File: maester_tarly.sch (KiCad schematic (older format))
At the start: 30 parts, among them J101 Micro_SD_Card_Det, J102 USB_B_Micro, J103 USB_A, J104 Conn_01x06, J105 Conn_01x10, J106 RJ45_Amphenol_RJMG1BD3B8K1ANR, J107 DF40GB(1.5)-48DS-0.4V, J108 DF40GB(1.5)-48DS-0.4V, J109 DF40GB(1.5)-48DS-0.4V, J110 DF40GB(1.5)-48DS-0.4V

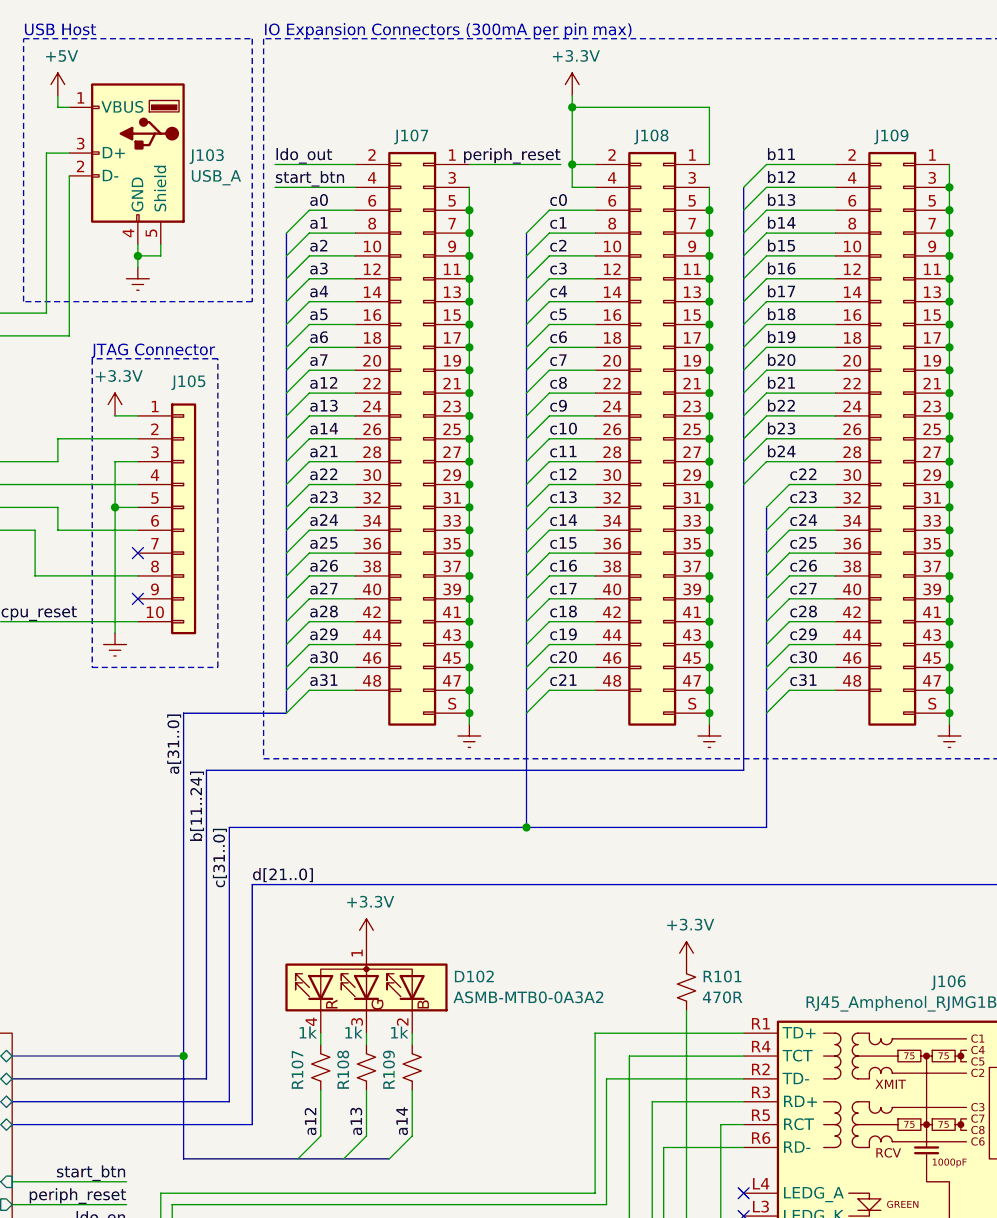
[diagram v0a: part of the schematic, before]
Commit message: Escaped all traced from the CPU
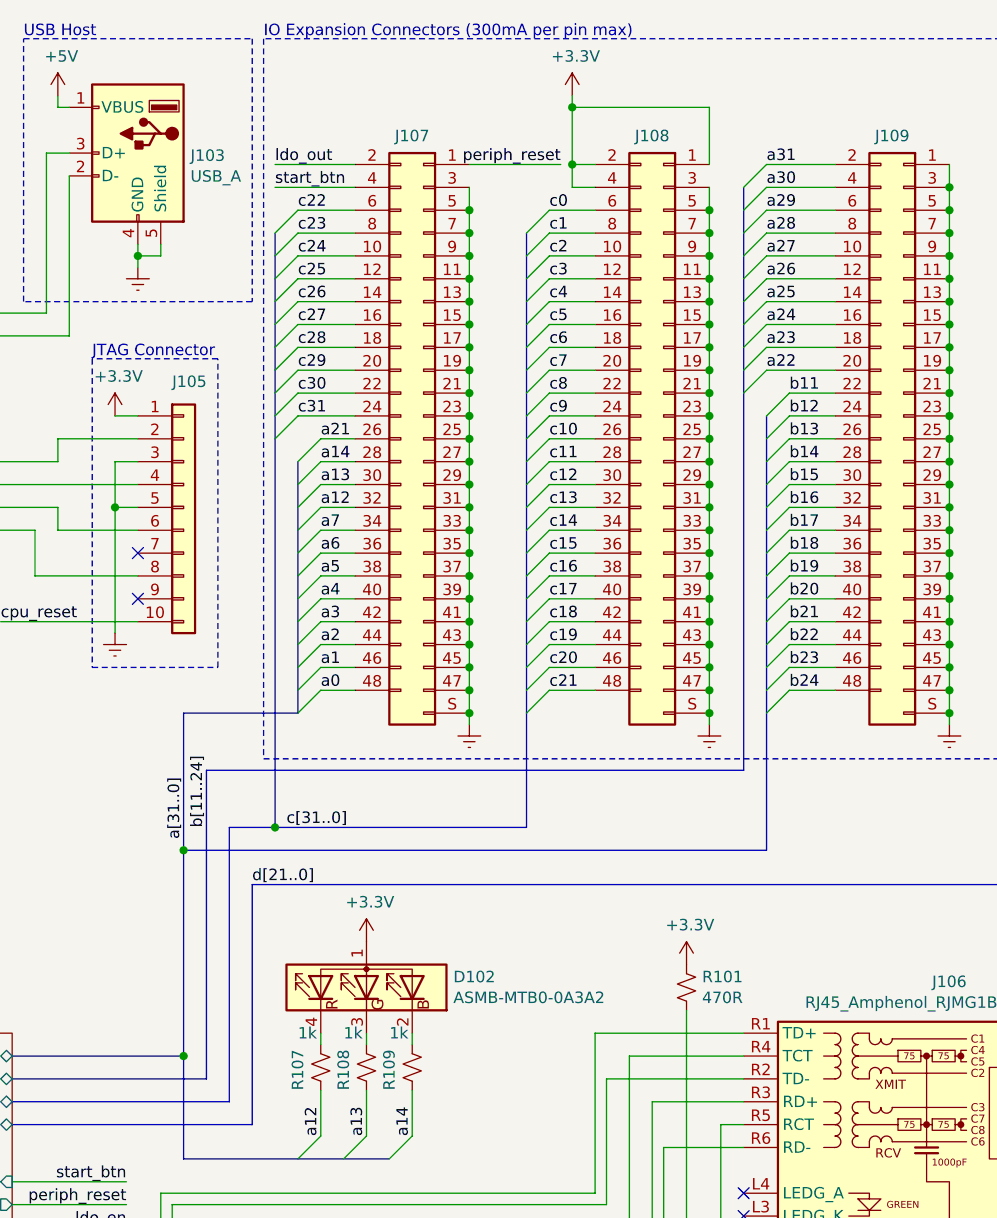
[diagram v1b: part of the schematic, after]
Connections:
- net a0: now also J107.48 (Pin_48); no longer J107.6 (Pin_6)
- net a1: now also J107.46 (Pin_46); no longer J107.8 (Pin_8)
- net a12: now also J107.32 (Pin_32); no longer J107.22 (Pin_22)
- net a13: now also J107.30 (Pin_30); no longer J107.24 (Pin_24)
- net a14: now also J107.28 (Pin_28); no longer J107.26 (Pin_26)
- net a2: now also J107.44 (Pin_44); no longer J107.10 (Pin_10)
- net a21: now also J107.26 (Pin_26); no longer J107.28 (Pin_28)
- net a22: now also J109.20 (Pin_20); no longer J107.30 (Pin_30)
- net a23: now also J109.18 (Pin_18); no longer J107.32 (Pin_32)
- net a24: now also J109.16 (Pin_16); no longer J107.34 (Pin_34)
- net a25: now also J109.14 (Pin_14); no longer J107.36 (Pin_36)
- net a26: now also J109.12 (Pin_12); no longer J107.38 (Pin_38)
- net a27: now also J109.10 (Pin_10); no longer J107.40 (Pin_40)
- net a28: now also J109.8 (Pin_8); no longer J107.42 (Pin_42)
- net a29: now also J109.6 (Pin_6); no longer J107.44 (Pin_44)
- net a3: now also J107.42 (Pin_42); no longer J107.12 (Pin_12)
- net a30: now also J109.4 (Pin_4); no longer J107.46 (Pin_46)
- net a31: now also J109.2 (Pin_2); no longer J107.48 (Pin_48)
- net a4: now also J107.40 (Pin_40); no longer J107.14 (Pin_14)
- net a5: now also J107.38 (Pin_38); no longer J107.16 (Pin_16)
- net a6: now also J107.36 (Pin_36); no longer J107.18 (Pin_18)
- net a7: now also J107.34 (Pin_34); no longer J107.20 (Pin_20)
- net b11: now also J109.22 (Pin_22); no longer J109.2 (Pin_2)
- net b12: now also J109.24 (Pin_24); no longer J109.4 (Pin_4)
- net b13: now also J109.26 (Pin_26); no longer J109.6 (Pin_6)
- net b14: now also J109.28 (Pin_28); no longer J109.8 (Pin_8)
- net b15: now also J109.30 (Pin_30); no longer J109.10 (Pin_10)
- net b16: now also J109.32 (Pin_32); no longer J109.12 (Pin_12)
- net b17: now also J109.34 (Pin_34); no longer J109.14 (Pin_14)
- net b18: now also J109.36 (Pin_36); no longer J109.16 (Pin_16)
- net b19: now also J109.38 (Pin_38); no longer J109.18 (Pin_18)
- net b20: now also J109.40 (Pin_40); no longer J109.20 (Pin_20)
- net b21: now also J109.42 (Pin_42); no longer J109.22 (Pin_22)
- net b22: now also J109.44 (Pin_44); no longer J109.24 (Pin_24)
- net b23: now also J109.46 (Pin_46); no longer J109.26 (Pin_26)
- net b24: now also J109.48 (Pin_48); no longer J109.28 (Pin_28)
- net c22: now also J107.6 (Pin_6); no longer J109.30 (Pin_30)
- net c23: now also J107.8 (Pin_8); no longer J109.32 (Pin_32)
- net c24: now also J107.10 (Pin_10); no longer J109.34 (Pin_34)
- net c25: now also J107.12 (Pin_12); no longer J109.36 (Pin_36)
- net c26: now also J107.14 (Pin_14); no longer J109.38 (Pin_38)
- net c27: now also J107.16 (Pin_16); no longer J109.40 (Pin_40)
- net c28: now also J107.18 (Pin_18); no longer J109.42 (Pin_42)
- net c29: now also J107.20 (Pin_20); no longer J109.44 (Pin_44)
- net c30: now also J107.22 (Pin_22); no longer J109.46 (Pin_46)
- net c31: now also J107.24 (Pin_24); no longer J109.48 (Pin_48)

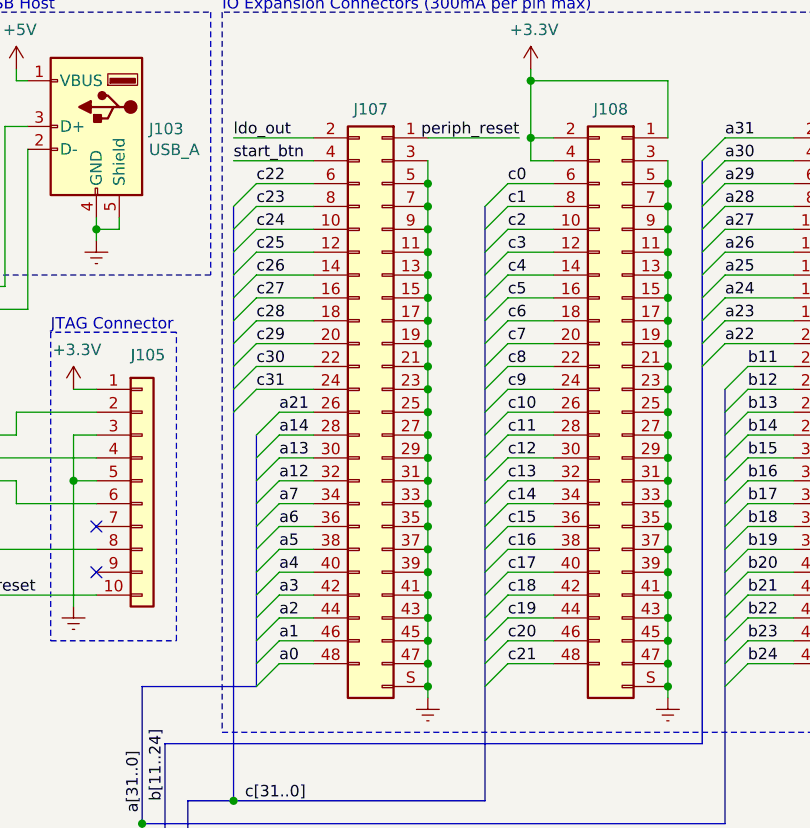
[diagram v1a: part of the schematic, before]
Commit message: Placed all the parts. Some will have to move.
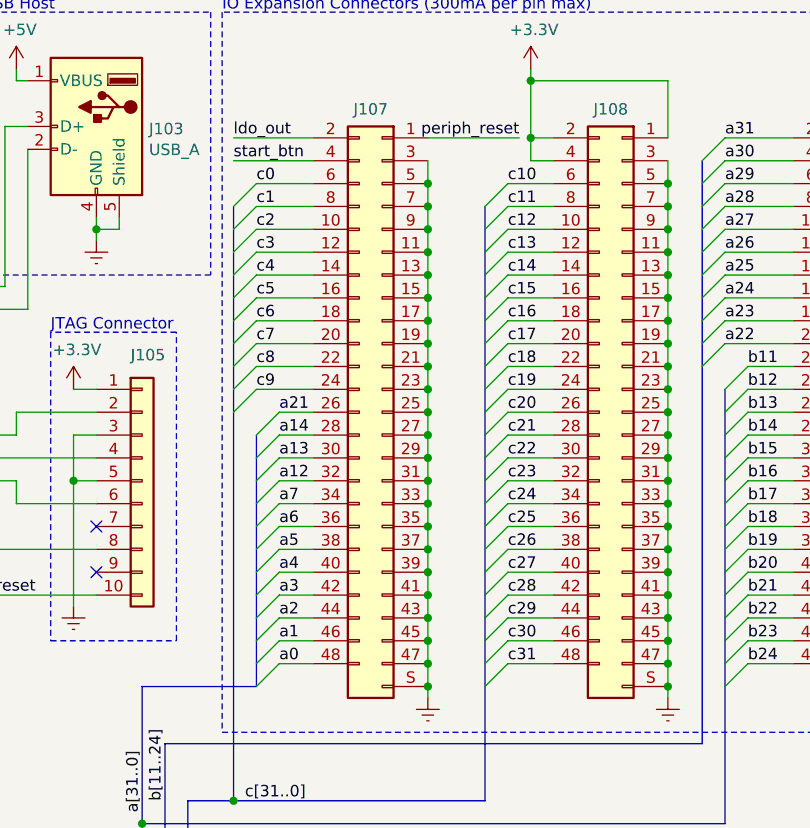
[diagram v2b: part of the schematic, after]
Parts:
- C102: footprint Capacitor_SMD:C_0402_1005Metric -> Capacitor_SMD:C_0805_2012Metric
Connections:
- net c0: now also J107.6 (Pin_6); no longer J108.6 (Pin_6)
- net c1: now also J107.8 (Pin_8); no longer J108.8 (Pin_8)
- net c10: now also J108.6 (Pin_6); no longer J108.26 (Pin_26)
- net c11: now also J108.8 (Pin_8); no longer J108.28 (Pin_28)
- net c12: now also J108.10 (Pin_10); no longer J108.30 (Pin_30)
- net c13: now also J108.12 (Pin_12); no longer J108.32 (Pin_32)
- net c14: now also J108.14 (Pin_14); no longer J108.34 (Pin_34)
- net c15: now also J108.16 (Pin_16); no longer J108.36 (Pin_36)
- net c16: now also J108.18 (Pin_18); no longer J108.38 (Pin_38)
- net c17: now also J108.20 (Pin_20); no longer J108.40 (Pin_40)
- net c18: now also J108.22 (Pin_22); no longer J108.42 (Pin_42)
- net c19: now also J108.24 (Pin_24); no longer J108.44 (Pin_44)
- net c2: now also J107.10 (Pin_10); no longer J108.10 (Pin_10)
- net c20: now also J108.26 (Pin_26); no longer J108.46 (Pin_46)
- net c21: now also J108.28 (Pin_28); no longer J108.48 (Pin_48)
- net c22: now also J108.30 (Pin_30); no longer J107.6 (Pin_6)
- net c23: now also J108.32 (Pin_32); no longer J107.8 (Pin_8)
- net c24: now also J108.34 (Pin_34); no longer J107.10 (Pin_10)
- net c25: now also J108.36 (Pin_36); no longer J107.12 (Pin_12)
- net c26: now also J108.38 (Pin_38); no longer J107.14 (Pin_14)
- net c27: now also J108.40 (Pin_40); no longer J107.16 (Pin_16)
- net c28: now also J108.42 (Pin_42); no longer J107.18 (Pin_18)
- net c29: now also J108.44 (Pin_44); no longer J107.20 (Pin_20)
- net c3: now also J107.12 (Pin_12); no longer J108.12 (Pin_12)
- net c30: now also J108.46 (Pin_46); no longer J107.22 (Pin_22)
- net c31: now also J108.48 (Pin_48); no longer J107.24 (Pin_24)
- net c4: now also J107.14 (Pin_14); no longer J108.14 (Pin_14)
- net c5: now also J107.16 (Pin_16); no longer J108.16 (Pin_16)
- net c6: now also J107.18 (Pin_18); no longer J108.18 (Pin_18)
- net c7: now also J107.20 (Pin_20); no longer J108.20 (Pin_20)
- net c8: now also J107.22 (Pin_22); no longer J108.22 (Pin_22)
- net c9: now also J107.24 (Pin_24); no longer J108.24 (Pin_24)
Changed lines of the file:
@@
 F 0 "C102" H 3392 5846 50  0000 L CNN
 F 1 "4.7uF" H 3392 5755 50  0000 L CNN
-F 2 "Capacitor_SMD:C_0402_1005Metric" H 3300 5800 50  0001 C CNN
+F 2 "Capacitor_SMD:C_0805_2012Metric" H 3300 5800 50  0001 C CNN
 F 3 "~" H 3300 5800 50  0001 C CNN
 	1    3300 5800
@@
 Text Label 6800 4100 1    50   ~ 0
 b[11..24]
+Text Label 7200 1400 0    50   ~ 0
+c0
+Text Label 7200 1500 0    50   ~ 0
+c1
+Text Label 7200 1600 0    50   ~ 0
+c2
+Text Label 7200 1700 0    50   ~ 0
+c3
+Text Label 7200 1800 0    50   ~ 0
+c4
+Text Label 7200 1900 0    50   ~ 0
+c5
+Text Label 7200 2000 0    50   ~ 0
+c6
+Text Label 7200 2100 0    50   ~ 0
+c7
+Text Label 7200 2200 0    50   ~ 0
+c8
+Text Label 7200 2300 0    50   ~ 0
+c9
 Text Label 8300 1400 0    50   ~ 0
-c0
+c10
 Text Label 8300 1500 0    50   ~ 0
-c1
+c11
 Text Label 8300 1600 0    50   ~ 0
-c2
+c12
 Text Label 8300 1700 0    50   ~ 0
-c3
+c13
 Text Label 8300 1800 0    50   ~ 0
-c4
+c14
 Text Label 8300 1900 0    50   ~ 0
-c5
+c15
 Text Label 8300 2000 0    50   ~ 0
-c6
+c16
 Text Label 8300 2100 0    50   ~ 0
-c7
+c17
 Text Label 8300 2200 0    50   ~ 0
-c8
+c18
 Text Label 8300 2300 0    50   ~ 0
-c9
+c19
 Text Label 8300 2400 0    50   ~ 0
-c10
+c20
 Text Label 8300 2500 0    50   ~ 0
-c11
-Text Label 8300 2600 0    50   ~ 0
-c12
-Text Label 8300 2700 0    50   ~ 0
-c13
-Text Label 8300 2800 0    50   ~ 0
-c14
-Text Label 8300 2900 0    50   ~ 0
-c15
-Text Label 8300 3000 0    50   ~ 0
-c16
-Text Label 8300 3100 0    50   ~ 0
-c17
-Text Label 8300 3200 0    50   ~ 0
-c18
-Text Label 8300 3300 0    50   ~ 0
-c19
-Text Label 8300 3400 0    50   ~ 0
-c20
-Text Label 8300 3500 0    50   ~ 0
 c21
-Text Label 7200 1400 0    50   ~ 0
-c22
-Text Label 7200 1500 0    50   ~ 0
-c23
-Text Label 7200 1600 0    50   ~ 0
-c24
-Text Label 7200 1700 0    50   ~ 0
-c25
-Text Label 7200 1800 0    50   ~ 0
-c26
-Text Label 7200 1900 0    50   ~ 0
-c27
-Text Label 7200 2000 0    50   ~ 0
-c28
-Text Label 7200 2100 0    50   ~ 0
-c29
-Text Label 7200 2200 0    50   ~ 0
-c30
-Text Label 7200 2300 0    50   ~ 0
-c31
 Wire Wire Line
 	6100 1150 6200 1150
@@
 	7450 3500 7300 3500
 Wire Wire Line
-	8500 3400 8300 3400
-Wire Wire Line
-	8500 3500 8300 3500
+	8500 2400 8300 2400
+Wire Wire Line
+	8500 2500 8300 2500
 Wire Wire Line
 	8500 1400 8300 1400
@@
 Wire Wire Line
 	8500 2300 8300 2300
-Wire Wire Line
-	8500 2400 8300 2400
-Wire Wire Line
-	8500 2500 8300 2500
-Wire Wire Line
-	8500 2600 8300 2600
-Wire Wire Line
-	8500 2700 8300 2700
-Wire Wire Line
-	8500 2800 8300 2800
-Wire Wire Line
-	8500 2900 8300 2900
-Wire Wire Line
-	8500 3000 8300 3000
-Wire Wire Line
-	8500 3100 8300 3100
-Wire Wire Line
-	8500 3200 8300 3200
-Wire Wire Line
-	8500 3300 8300 3300
 Entry Wire Line
 	9150 1900 9250 1800
@@
 	9150 2000 9250 1900
 Entry Wire Line
+	7100 1500 7200 1400
+Entry Wire Line
+	7100 1600 7200 1500
+Entry Wire Line
+	7100 1700 7200 1600
+Entry Wire Line
+	7100 1800 7200 1700
+Entry Wire Line
+	7100 1900 7200 1800
+Entry Wire Line
+	7100 2000 7200 1900
+Entry Wire Line
+	7100 2100 7200 2000
+Entry Wire Line
+	7100 2200 7200 2100
+Entry Wire Line
+	7100 2300 7200 2200
+Entry Wire Line
+	7100 2400 7200 2300
+Entry Wire Line
 	8200 1500 8300 1400
 Entry Wire Line
@@
 	8200 2400 8300 2300
 Entry Wire Line
+	7200 2500 7300 2400
+Entry Wire Line
+	7200 2600 7300 2500
+Entry Wire Line
+	7200 2700 7300 2600
+Entry Wire Line
+	7200 2800 7300 2700
+Entry Wire Line
+	7200 2900 7300 2800
+Entry Wire Line
+	7200 3000 7300 2900
+Entry Wire Line
+	7200 3100 7300 3000
+Entry Wire Line
+	7200 3200 7300 3100
+Entry Wire Line
+	7200 3300 7300 3200
+Entry Wire Line
+	7200 3400 7300 3300
+Entry Wire Line
+	7200 3500 7300 3400
+Entry Wire Line
+	7200 3600 7300 3500
+Entry Wire Line
 	8200 2500 8300 2400
 Entry Wire Line
 	8200 2600 8300 2500
-Entry Wire Line
-	8200 2700 8300 2600
-Entry Wire Line
-	8200 2800 8300 2700
-Entry Wire Line
-	8200 2900 8300 2800
-Entry Wire Line
-	8200 3000 8300 2900
-Entry Wire Line
-	8200 3100 8300 3000
-Entry Wire Line
-	8200 3200 8300 3100
-Entry Wire Line
-	8200 3300 8300 3200
-Entry Wire Line
-	8200 3400 8300 3300
-Entry Wire Line
-	7200 2500 7300 2400
-Entry Wire Line
-	7200 2600 7300 2500
-Entry Wire Line
-	7200 2700 7300 2600
-Entry Wire Line
-	7200 2800 7300 2700
-Entry Wire Line
-	7200 2900 7300 2800
-Entry Wire Line
-	7200 3000 7300 2900
-Entry Wire Line
-	7200 3100 7300 3000
-Entry Wire Line
-	7200 3200 7300 3100
-Entry Wire Line
-	7200 3300 7300 3200
-Entry Wire Line
-	7200 3400 7300 3300
-Entry Wire Line
-	7200 3500 7300 3400
-Entry Wire Line
-	7200 3600 7300 3500
-Entry Wire Line
-	8200 3500 8300 3400
-Entry Wire Line
-	8200 3600 8300 3500
-Entry Wire Line
-	7100 1500 7200 1400
-Entry Wire Line
-	7100 1600 7200 1500
-Entry Wire Line
-	7100 1700 7200 1600
-Entry Wire Line
-	7100 1800 7200 1700
-Entry Wire Line
-	7100 1900 7200 1800
-Entry Wire Line
-	7100 2000 7200 1900
-Entry Wire Line
-	7100 2100 7200 2000
-Entry Wire Line
-	7100 2200 7200 2100
-Entry Wire Line
-	7100 2300 7200 2200
-Entry Wire Line
-	7100 2400 7200 2300
 Entry Wire Line
 	10300 1500 10400 1400
@@
 	5950 5300 6900 5300
 Wire Bus Line
-	6900 4100 7100 4100
-Wire Bus Line
 	5950 5200 6800 5200
 Wire Bus Line
@@
 Text Label 7300 2400 0    50   ~ 0
 a21
-Wire Wire Line
-	7200 1400 7450 1400
-Wire Wire Line
-	7200 1500 7450 1500
-Wire Wire Line
-	7200 1600 7450 1600
-Wire Wire Line
-	7200 1700 7450 1700
-Wire Wire Line
-	7200 1800 7450 1800
-Wire Wire Line
-	7200 1900 7450 1900
-Wire Wire Line
-	7200 2000 7450 2000
-Wire Wire Line
-	7200 2100 7450 2100
-Wire Wire Line
-	7200 2200 7450 2200
-Wire Wire Line
-	7200 2300 7450 2300
-Connection ~ 7100 4100
-Wire Bus Line
-	7100 4100 8200 4100
 Wire Bus Line
 	9250 4200 6700 4200
@@
 Wire Wire Line
 	9250 2100 9550 2100
+Connection ~ 7100 4100
+Wire Bus Line
+	7100 4100 8200 4100
+Wire Bus Line
+	6900 4100 7100 4100
+Wire Wire Line
+	8300 3500 8500 3500
+Wire Wire Line
+	8300 3400 8500 3400
+Wire Wire Line
+	8300 3300 8500 3300
+Wire Wire Line
+	8300 3200 8500 3200
+Wire Wire Line
+	8300 3100 8500 3100
+Wire Wire Line
+	8300 3000 8500 3000
+Wire Wire Line
+	8300 2900 8500 2900
+Wire Wire Line
+	8300 2800 8500 2800
+Wire Wire Line
+	8300 2700 8500 2700
+Wire Wire Line
+	8300 2600 8500 2600
+Entry Wire Line
+	8200 3600 8300 3500
+Entry Wire Line
+	8200 3500 8300 3400
+Entry Wire Line
+	8200 3400 8300 3300
+Entry Wire Line
+	8200 3300 8300 3200
+Entry Wire Line
+	8200 3200 8300 3100
+Entry Wire Line
+	8200 3100 8300 3000
+Entry Wire Line
+	8200 3000 8300 2900
+Entry Wire Line
+	8200 2900 8300 2800
+Entry Wire Line
+	8200 2800 8300 2700
+Entry Wire Line
+	8200 2700 8300 2600
+Text Label 8300 3500 0    50   ~ 0
+c31
+Text Label 8300 3400 0    50   ~ 0
+c30
+Text Label 8300 3300 0    50   ~ 0
+c29
+Text Label 8300 3200 0    50   ~ 0
+c28
+Text Label 8300 3100 0    50   ~ 0
+c27
+Text Label 8300 3000 0    50   ~ 0
+c26
+Text Label 8300 2900 0    50   ~ 0
+c25
+Text Label 8300 2800 0    50   ~ 0
+c24
+Text Label 8300 2700 0    50   ~ 0
+c23
+Text Label 8300 2600 0    50   ~ 0
+c22
+Wire Wire Line
+	7200 1400 7450 1400
+Wire Wire Line
+	7200 1500 7450 1500
+Wire Wire Line
+	7200 1600 7450 1600
+Wire Wire Line
+	7200 1700 7450 1700
+Wire Wire Line
+	7200 1800 7450 1800
+Wire Wire Line
+	7200 1900 7450 1900
+Wire Wire Line
+	7200 2000 7450 2000
+Wire Wire Line
+	7200 2100 7450 2100
+Wire Wire Line
+	7200 2200 7450 2200
+Wire Wire Line
+	7200 2300 7450 2300
 Wire Bus Line
 	2950 5200 2950 5900
